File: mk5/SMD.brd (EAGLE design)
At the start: 31.9 x 37.7 mm, 12 parts, among them IC2 78L05F

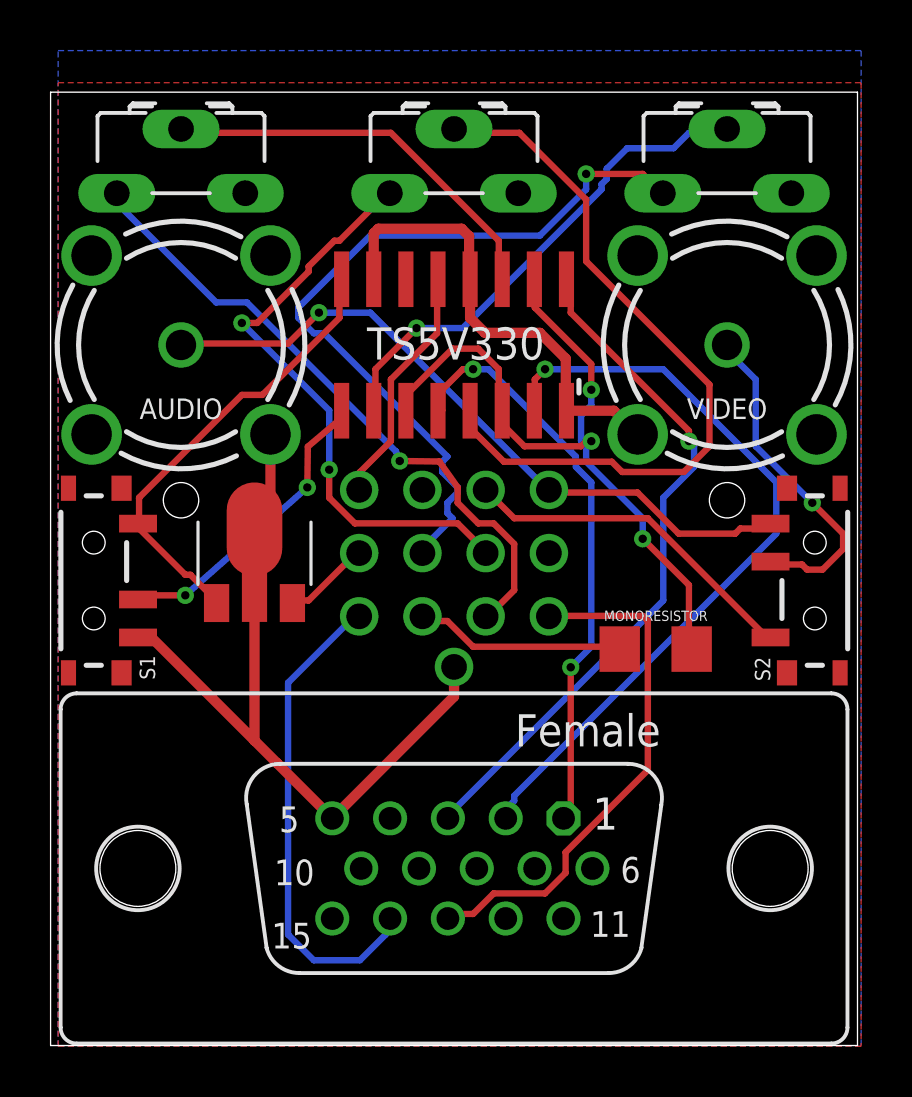
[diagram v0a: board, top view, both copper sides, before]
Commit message: Swapped switch pins on A/V switch, to make it easier to patch video to video RCA.
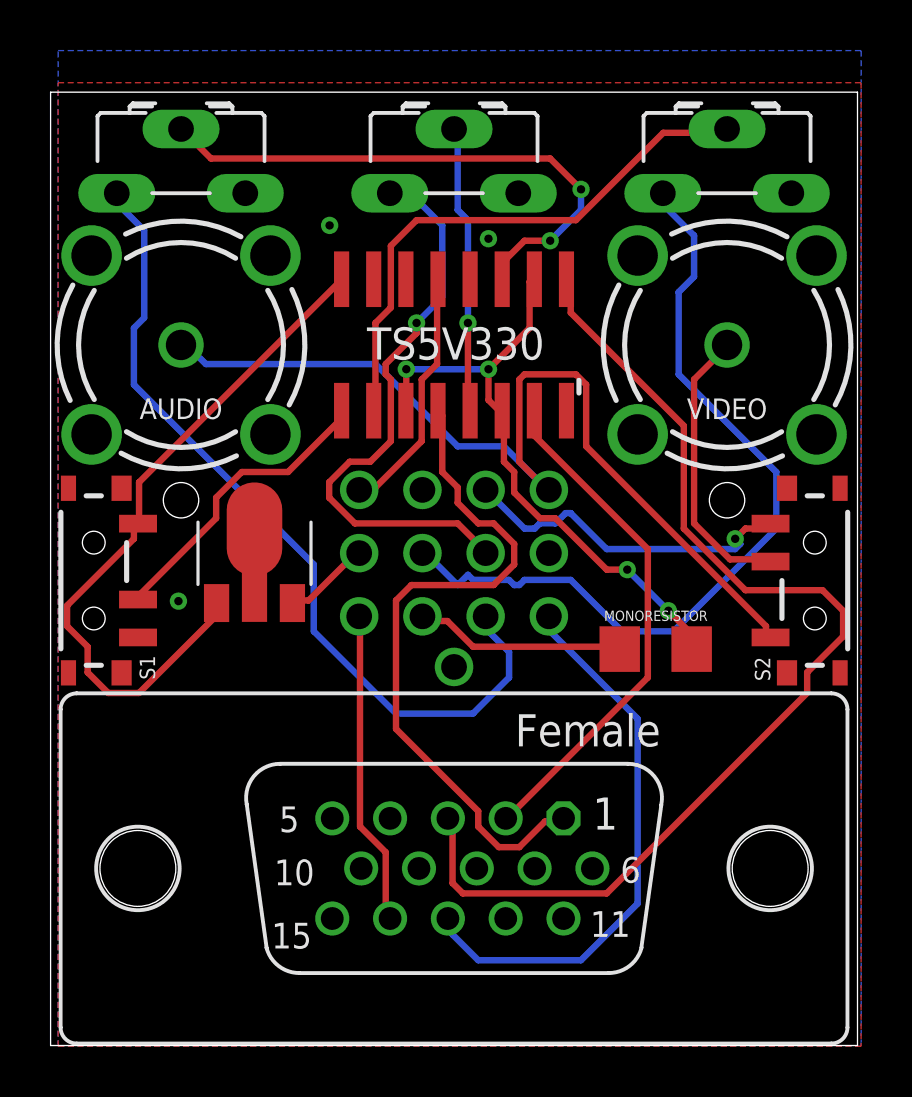
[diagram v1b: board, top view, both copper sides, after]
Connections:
- net AAUDIO: now also S2.3; no longer S2.1
- net AVIDEO: now also S2.1; no longer S2.3
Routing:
- net GND: track 49.7 -> 0.00 mm, vias 0 -> 3
- net GOUT: track 29.4 -> 11.4 mm, vias 0 -> 1
- net VBLUE: track 27.5 -> 43.4 mm, vias 1 -> 0
- net VGREEN: track 30.6 -> 20.3 mm, vias 1 -> 0
- net AAUDIO: track 27.6 -> 37.7 mm, vias 1 -> 0
- net +5V: track 18.0 -> 27.6 mm
- net ABLUE: track 25.6 -> 33.3 mm, vias 1 -> 0
- net AVSYNC: track 19.3 -> 12.4 mm
- net BOUT: track 16.0 -> 22.2 mm, vias 0 -> 2
- net MONOSIGNAL: track 29.5 -> 24.5 mm, vias 3 -> 4
- net VRED: track 23.0 -> 27.4 mm, vias 2 -> 0
- net ARED: track 30.7 -> 33.1 mm, vias 1 -> 0
- net A/V-PIN: track 13.4 -> 11.2 mm, vias 1 -> 0
- net ROUT: track 19.9 -> 22.1 mm, vias 1 -> 0
- net AHSYNC: track 20.7 -> 22.3 mm
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
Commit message: Better placement of vias, to minimize risk of bridging.
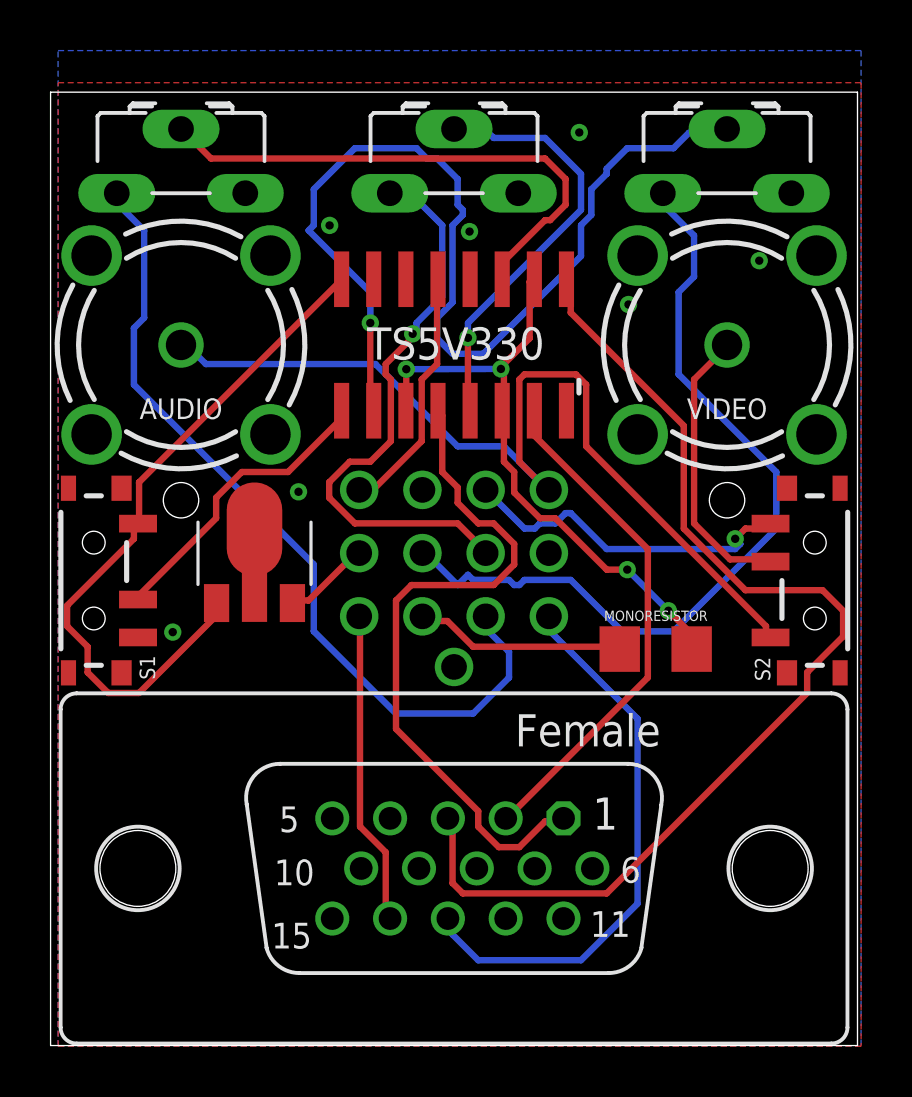
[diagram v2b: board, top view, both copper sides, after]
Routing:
- net ROUT: track 22.1 -> 40.5 mm, vias 0 -> 1
- net GOUT: track 11.4 -> 17.0 mm
- net BOUT: track 22.2 -> 21.1 mm, vias 2 -> 0
- net GND: track 0.00 -> 1.05 mm, vias 3 -> 7
